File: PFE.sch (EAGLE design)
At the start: 90 parts, among them IC1 74HC14N, IC2 74HC245N, K1 CQ1-12V, T1 BTA316-600B, T2 BTA316-600B, T3 2N2219

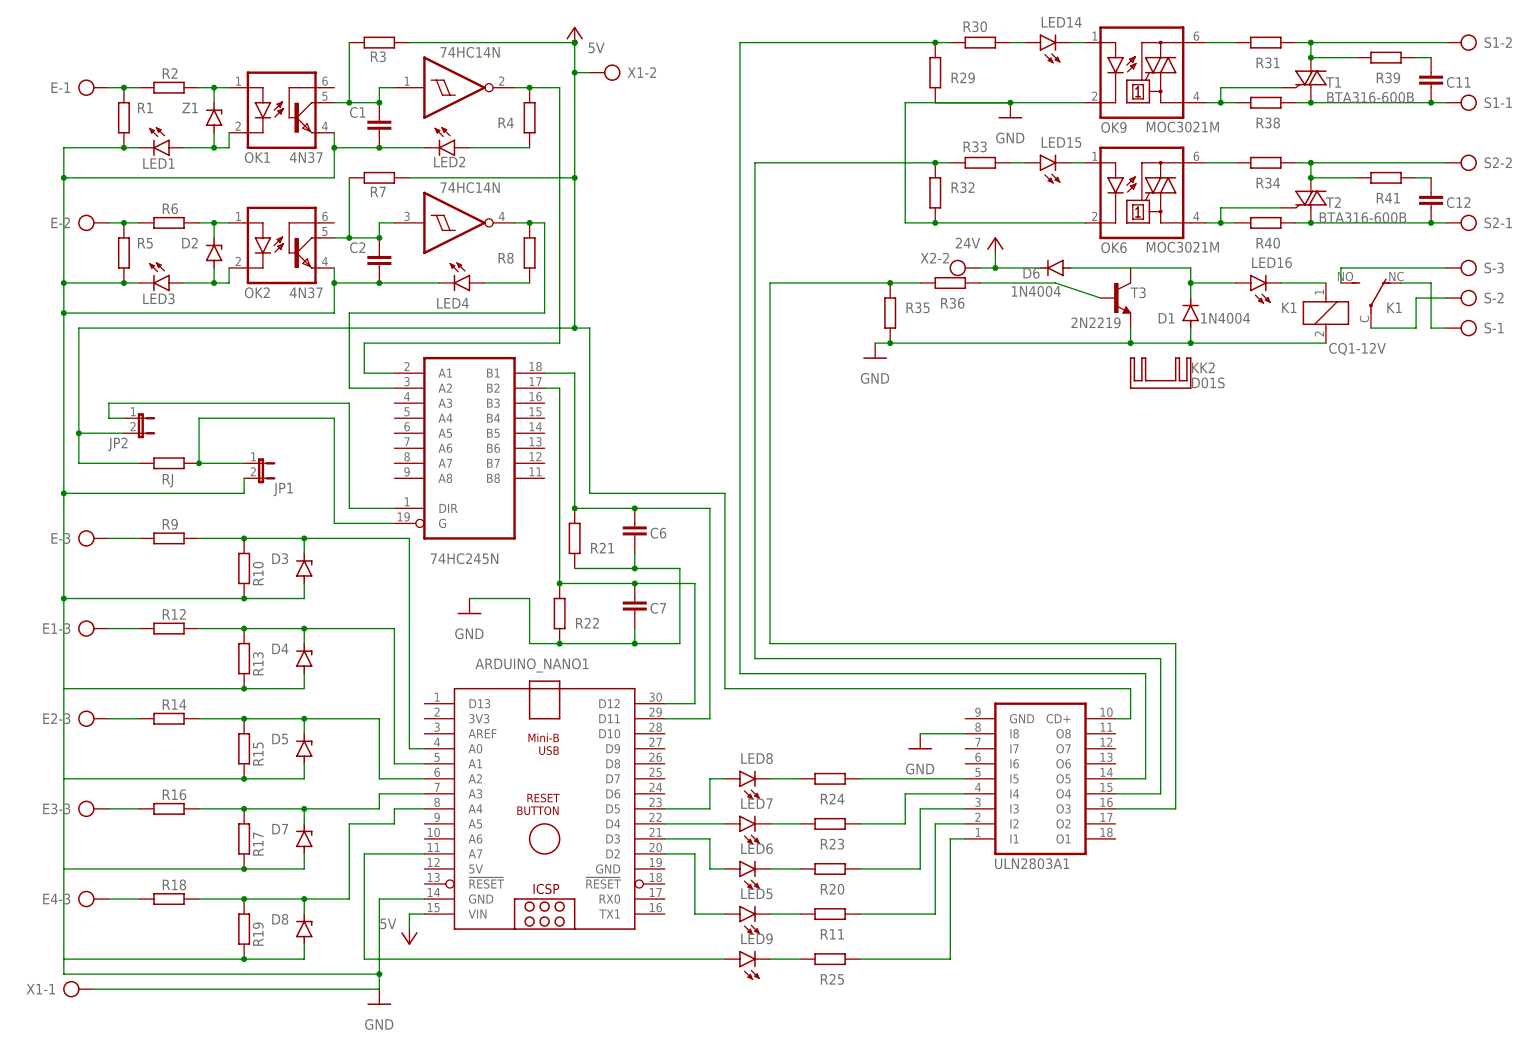
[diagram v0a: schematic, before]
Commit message: added the third triac output
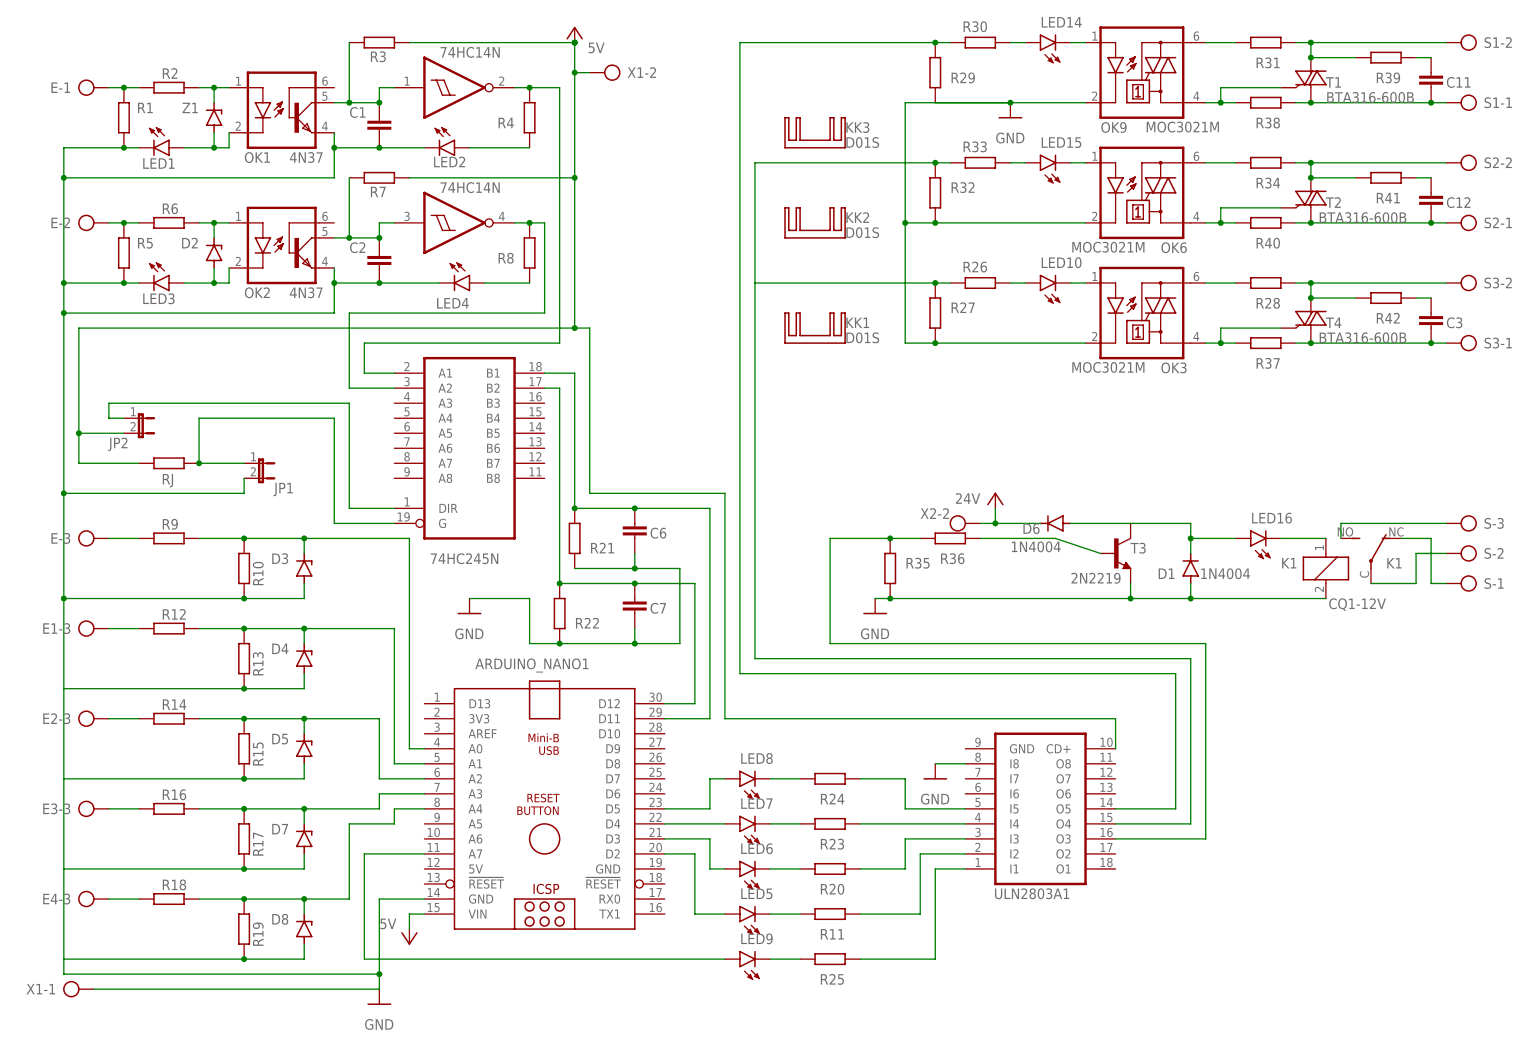
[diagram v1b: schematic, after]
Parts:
- added C3: (no value), rcl:C-EU075-052X106
- added KK1, KK3: D01S, heatsink:D01S
- added LED10: TLLY4400, led:TLLY4400
- added OK3: MOC3021M, optocoupler:MOC3021M
- added R26, R27, R28, R37, R42: (no value), rcl:R-EU_0204/7
- added S3: (no value), con-ptr500:AK300/2
- added T4: BTA316-600B, nxp_60:BTA316-600B
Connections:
- new net N$14: R28.2, R42.1, S3-2.KL, T4.LD
- new net N$17: LED10.A, R26.2
- new net N$33: LED10.C, OK3.A
- new net N$37: OK3.A2, R28.1
- new net N$5: C3.2, R37.2, S3-1.KL, T4.CM
- new net N$54: C3.1, R42.2
- new net N$69: OK3.A1, R37.1, T4.G
- new net N$72: R26.1, R27.2
- net GND: now also OK3.C, R27.1
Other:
- moved on the sheet: D1, D6, K1, KK2, LED16, R35, R36, S-1, S-2, S-3, T3, ULN2803A1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

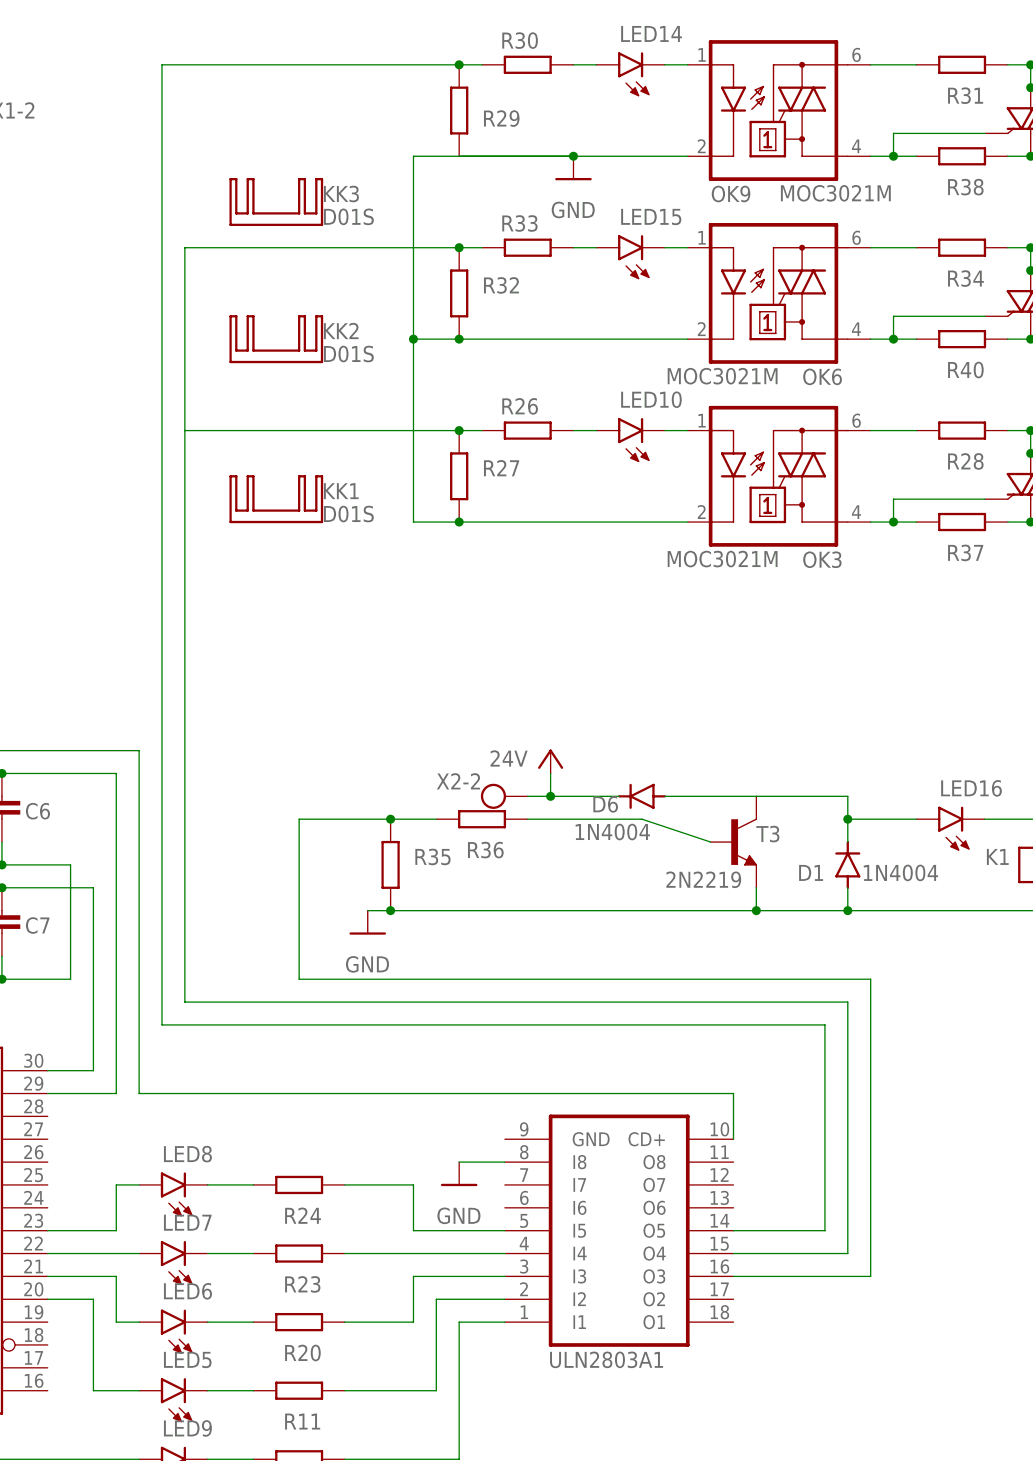
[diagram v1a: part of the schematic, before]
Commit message: added the third triac output
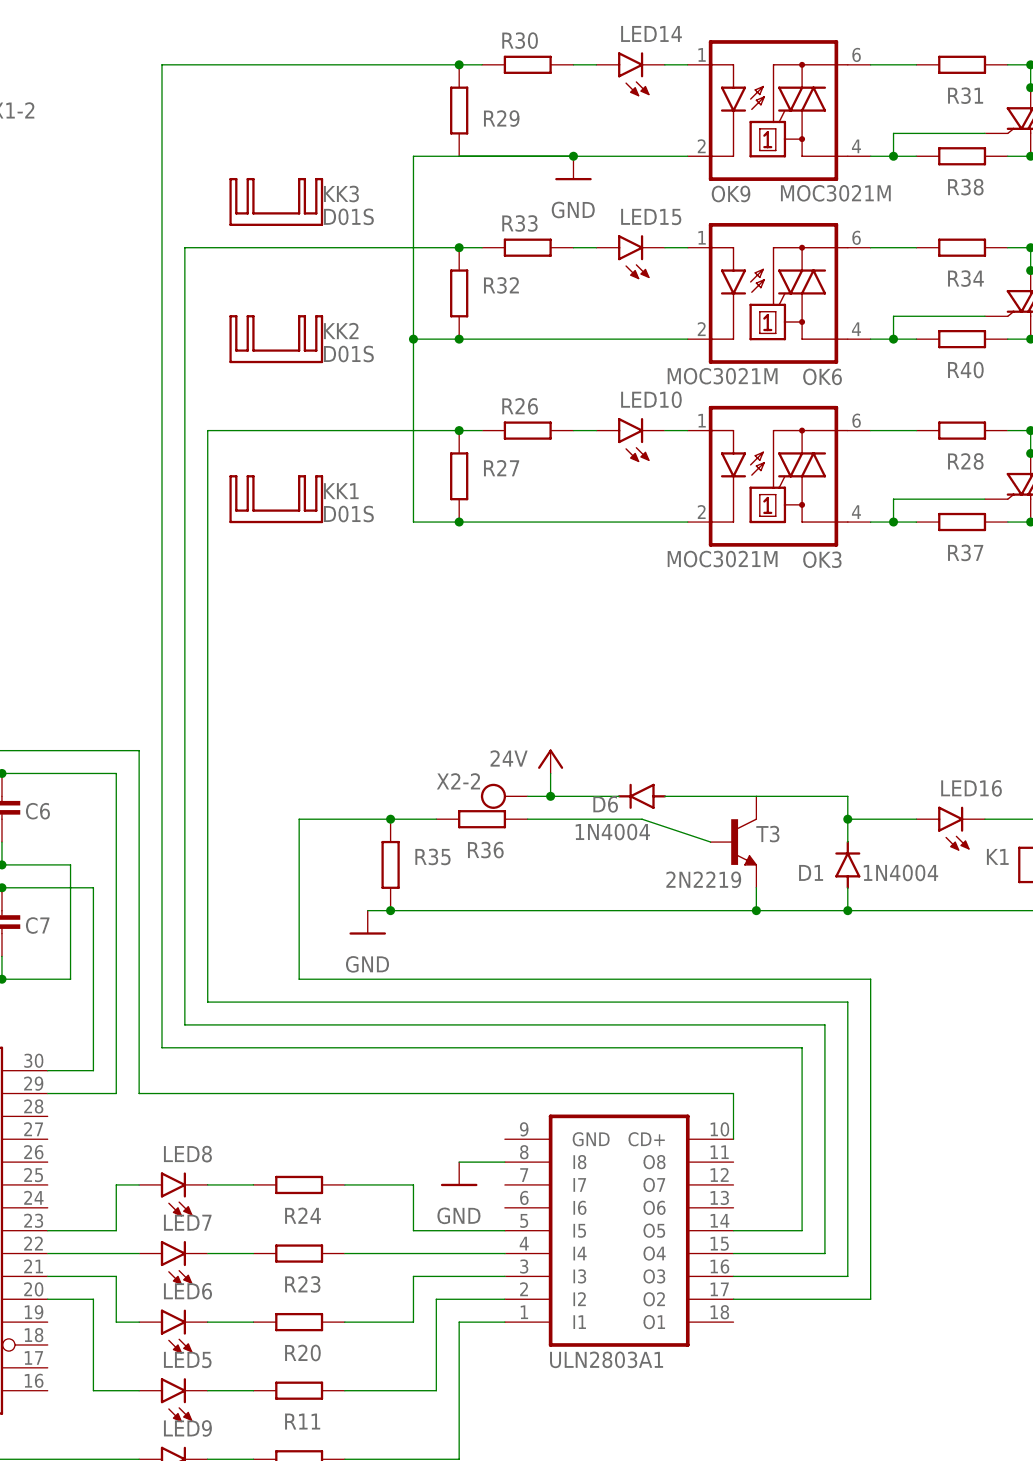
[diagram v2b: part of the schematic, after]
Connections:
- net N$55: now also ULN2803A1.O2; no longer ULN2803A1.O3
- net N$72: now also ULN2803A1.O3
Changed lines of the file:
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@@
 <wire x1="137.16" y1="86.36" x2="137.16" y2="68.58" width="0.1524" layer="91"/>
 <wire x1="137.16" y1="68.58" x2="200.66" y2="68.58" width="0.1524" layer="91"/>
-<wire x1="200.66" y1="68.58" x2="200.66" y2="35.56" width="0.1524" layer="91"/>
-<pinref part="ULN2803A1" gate="G$1" pin="O3"/>
-<wire x1="200.66" y1="35.56" x2="185.42" y2="35.56" width="0.1524" layer="91"/>
+<wire x1="200.66" y1="68.58" x2="200.66" y2="33.02" width="0.1524" layer="91"/>
+<pinref part="ULN2803A1" gate="G$1" pin="O2"/>
+<wire x1="185.42" y1="33.02" x2="200.66" y2="33.02" width="0.1524" layer="91"/>
 </segment>
 </net>
@@
 <wire x1="154.94" y1="170.18" x2="121.92" y2="170.18" width="0.1524" layer="91"/>
 <junction x="154.94" y="170.18"/>
-<wire x1="121.92" y1="170.18" x2="121.92" y2="63.5" width="0.1524" layer="91"/>
-<wire x1="121.92" y1="63.5" x2="195.58" y2="63.5" width="0.1524" layer="91"/>
-<wire x1="195.58" y1="63.5" x2="195.58" y2="40.64" width="0.1524" layer="91"/>
+<wire x1="121.92" y1="170.18" x2="121.92" y2="60.96" width="0.1524" layer="91"/>
+<wire x1="121.92" y1="60.96" x2="193.04" y2="60.96" width="0.1524" layer="91"/>
+<wire x1="193.04" y1="60.96" x2="193.04" y2="40.64" width="0.1524" layer="91"/>
 <pinref part="ULN2803A1" gate="G$1" pin="O5"/>
-<wire x1="195.58" y1="40.64" x2="185.42" y2="40.64" width="0.1524" layer="91"/>
+<wire x1="193.04" y1="40.64" x2="185.42" y2="40.64" width="0.1524" layer="91"/>
 </segment>
 </net>
@@
 <junction x="154.94" y="149.86"/>
 <wire x1="154.94" y1="149.86" x2="124.46" y2="149.86" width="0.1524" layer="91"/>
-<wire x1="124.46" y1="149.86" x2="124.46" y2="66.04" width="0.1524" layer="91"/>
-<wire x1="124.46" y1="66.04" x2="198.12" y2="66.04" width="0.1524" layer="91"/>
-<wire x1="198.12" y1="66.04" x2="198.12" y2="38.1" width="0.1524" layer="91"/>
+<wire x1="124.46" y1="149.86" x2="124.46" y2="63.5" width="0.1524" layer="91"/>
+<wire x1="124.46" y1="63.5" x2="195.58" y2="63.5" width="0.1524" layer="91"/>
+<wire x1="195.58" y1="63.5" x2="195.58" y2="38.1" width="0.1524" layer="91"/>
 <pinref part="ULN2803A1" gate="G$1" pin="O4"/>
-<wire x1="198.12" y1="38.1" x2="185.42" y2="38.1" width="0.1524" layer="91"/>
+<wire x1="195.58" y1="38.1" x2="185.42" y2="38.1" width="0.1524" layer="91"/>
 </segment>
 </net>
@@
 <pinref part="R27" gate="G$1" pin="2"/>
 <wire x1="154.94" y1="129.54" x2="157.48" y2="129.54" width="0.1524" layer="91"/>
+<wire x1="154.94" y1="129.54" x2="127" y2="129.54" width="0.1524" layer="91"/>
 <junction x="154.94" y="129.54"/>
-<wire x1="154.94" y1="129.54" x2="124.46" y2="129.54" width="0.1524" layer="91"/>
-</segment>
-</net>
+<wire x1="127" y1="129.54" x2="127" y2="66.04" width="0.1524" layer="91"/>
+<wire x1="127" y1="66.04" x2="198.12" y2="66.04" width="0.1524" layer="91"/>
+<wire x1="198.12" y1="66.04" x2="198.12" y2="35.56" width="0.1524" layer="91"/>
+<pinref part="ULN2803A1" gate="G$1" pin="O3"/>
+<wire x1="198.12" y1="35.56" x2="185.42" y2="35.56" width="0.1524" layer="91"/>
+</segment>
+</net>

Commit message: added the third triac output
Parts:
- removed E, E1, E2, E3, E4: (no value), con-ptr500:AK300/5
- added X3, X4, X5, X6: (no value), con-ptr500:AK300/2
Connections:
- net GND: now also X6-2.KL
- net N$1: now also X3-1.KL; no longer E-1.KL
- net N$13: now also X4-1.KL; no longer E-3.KL
- net N$16: now also X4-2.KL; no longer E1-3.KL
- net N$21: now also X5-1.KL; no longer E2-3.KL
- net N$23: now also X5-2.KL; no longer E3-3.KL
- net N$27: now also X6-1.KL; no longer E4-3.KL
- net N$8: now also X3-2.KL; no longer E-2.KL
